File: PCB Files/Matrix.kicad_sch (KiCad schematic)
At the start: 64 parts

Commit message: Change MX32 to 1.25U in the schematic
No real changes to production files
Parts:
- MX32: footprint MX_Only:MXOnly-1U-NoLED -> MX_Only:MXOnly-1.25U-NoLED
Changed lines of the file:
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@@
       (effects (font (size 0.508 0.508)) (justify left))
     )
-    (property "Footprint" "MX_Only:MXOnly-1U-NoLED" (id 2) (at 156.591 149.098 0)
+    (property "Footprint" "MX_Only:MXOnly-1.25U-NoLED" (id 2) (at 156.591 149.098 0)
       (effects (font (size 1.524 1.524)) hide)
     )

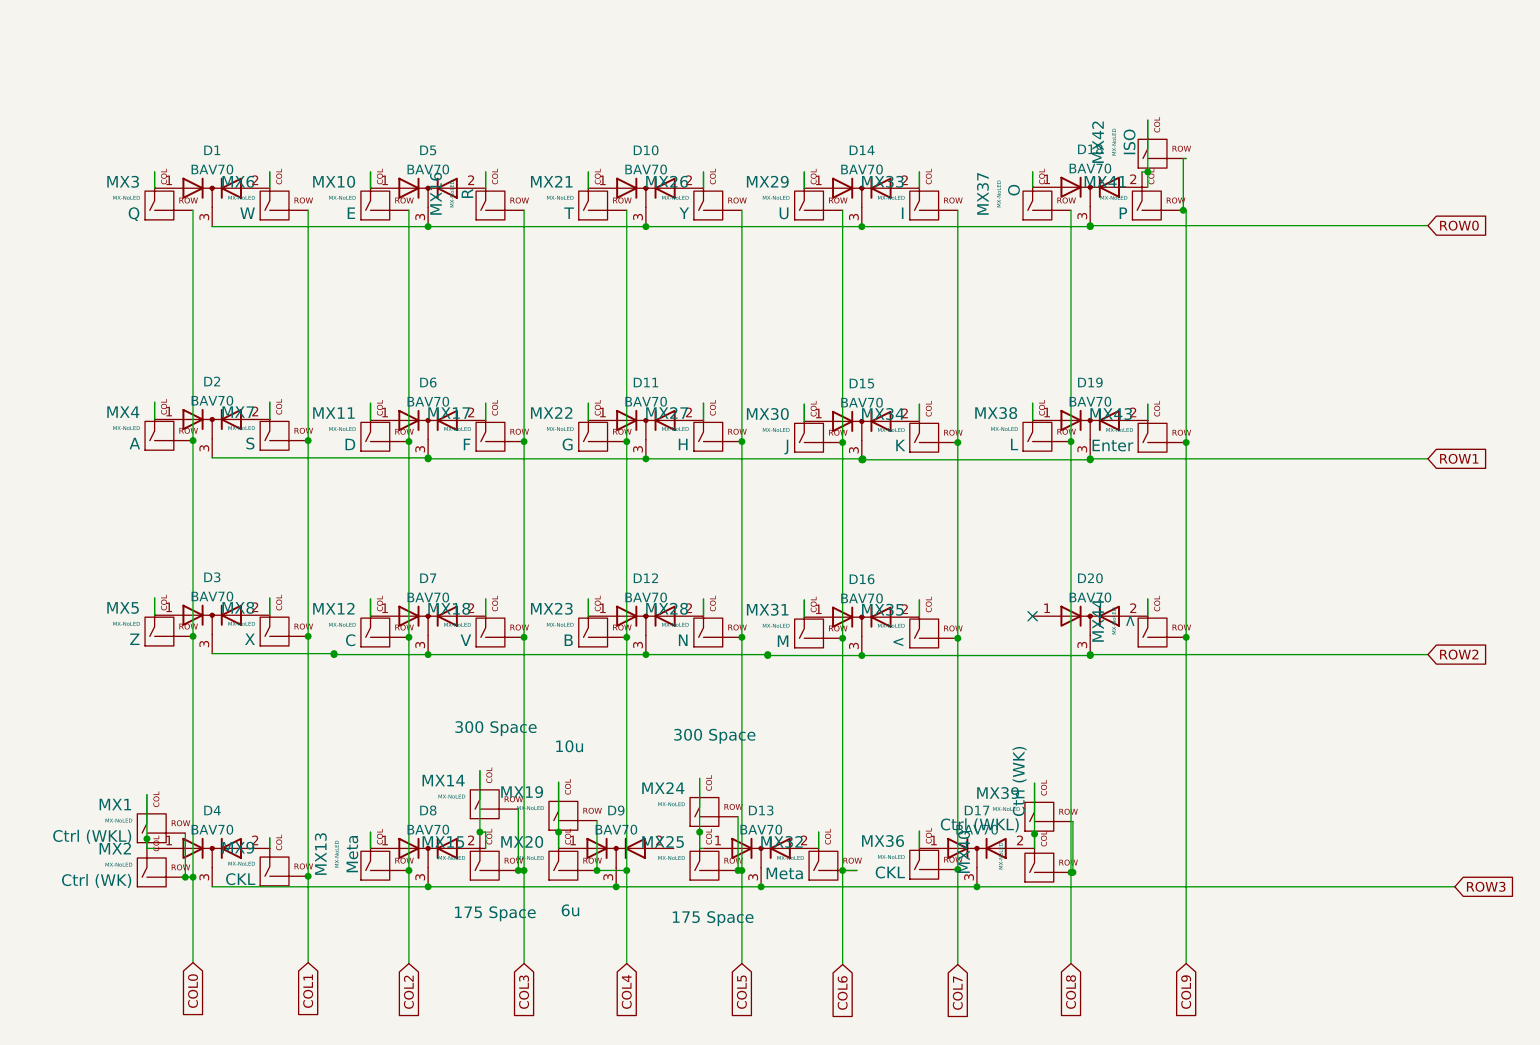
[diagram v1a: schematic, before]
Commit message: Cleanup the schematics and add a library for smaller bav70s
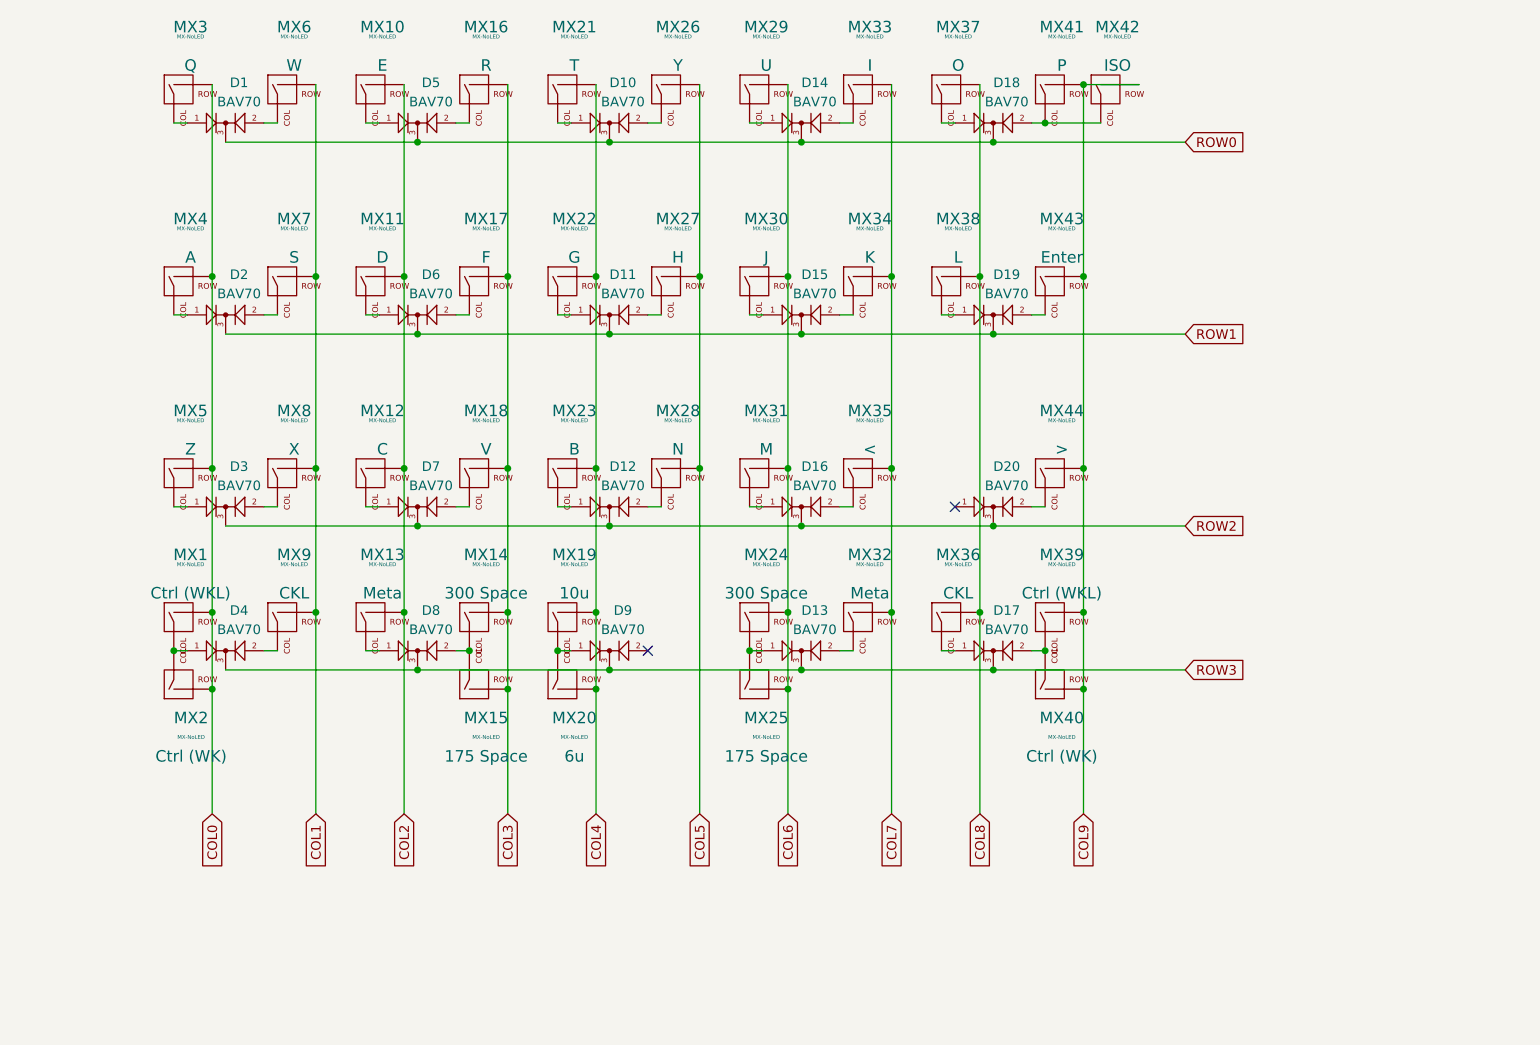
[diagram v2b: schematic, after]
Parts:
- D1, D10, D11, D12, D13, D14, D15, D16, D17, D18, D19, D2, D20, D3, D4, D5, D6, D7, D8, D9: symbol Diode:BAV70 -> marbastlib-various:BAV70_Small
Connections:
- net COL5: no longer MX24.2 (ROW), MX25.2 (ROW)
- net COL6: now also MX24.2 (ROW), MX25.2 (ROW); no longer MX32.2 (ROW)
- net COL7: now also MX32.2 (ROW); no longer MX36.2 (ROW)
- net COL8: now also MX36.2 (ROW); no longer MX39.2 (ROW), MX40.2 (ROW)
- net COL9: now also MX39.2 (ROW), MX40.2 (ROW)
- no-connect marks 1 -> 2
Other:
- moved on the sheet: MX1, MX10, MX11, MX12, MX13, MX14, MX15, MX16, MX17, MX18, MX19, MX2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

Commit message: Update dump
- Fix bottom row layout
- Add copium to dubba 1.75u shift using 1.5u and 1.25u
- Uglify @ASH-ART's routing
- Generate gerbers as recommended by JLC
- Add a logotype and revision number
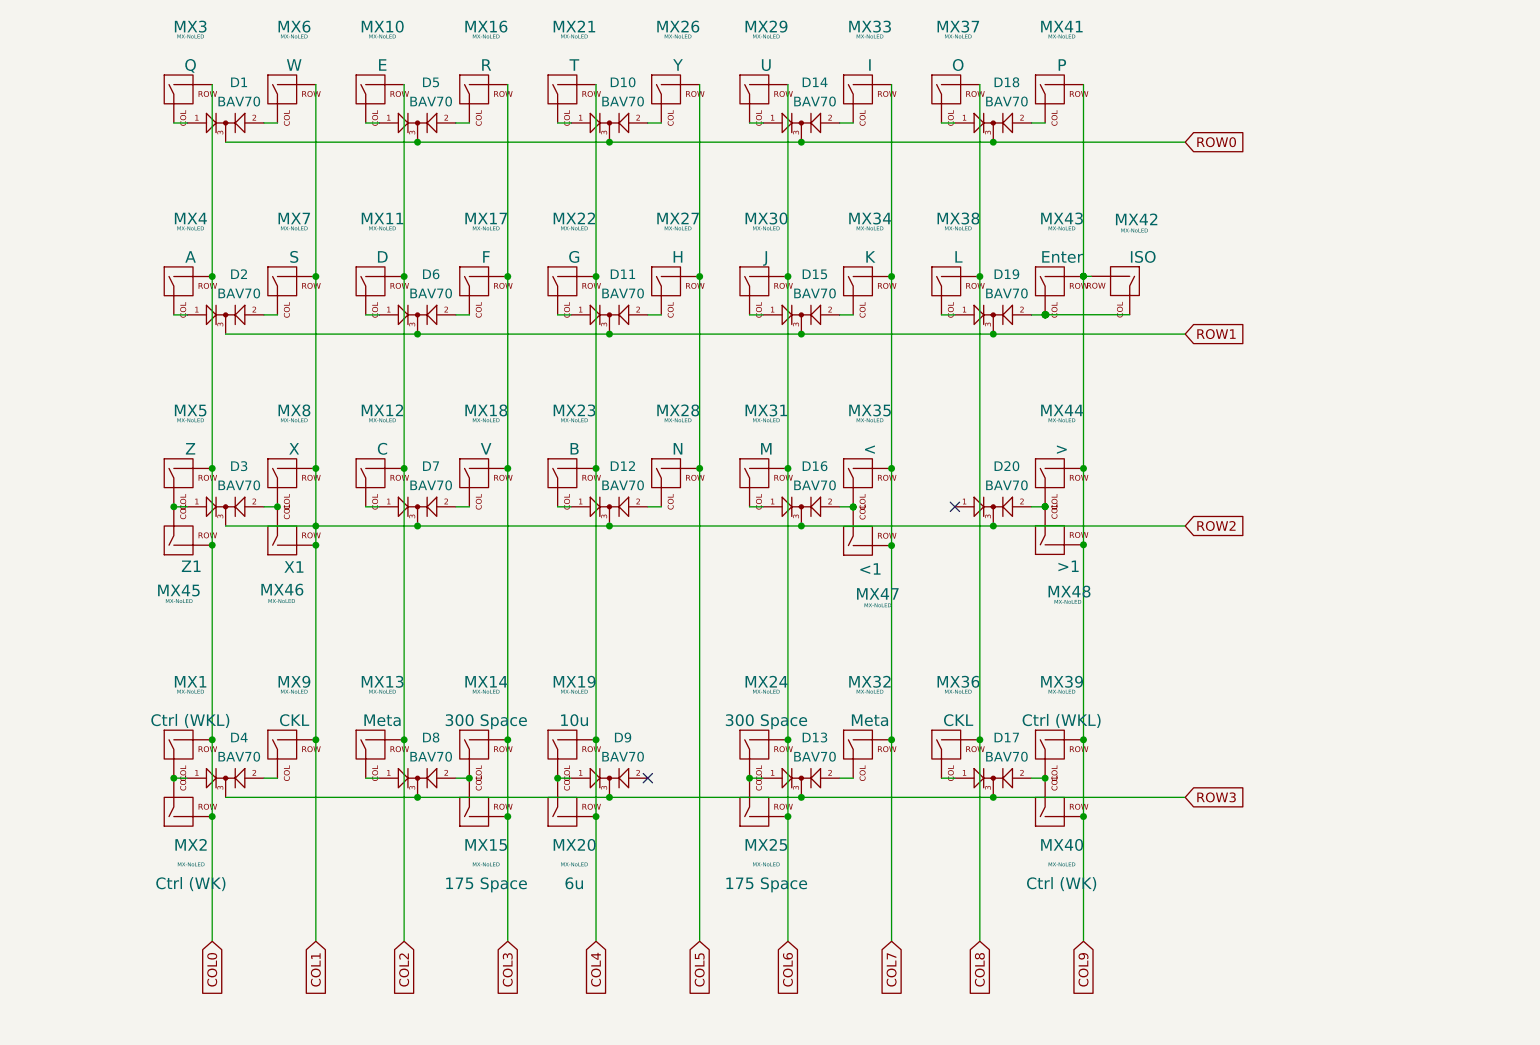
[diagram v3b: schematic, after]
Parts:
- added MX45, MX48: MX-NoLED, MX_Only:MXOnly-1.5U-NoLED, symbol MX_Alps_Hybrid:MX-NoLED
- added MX46, MX47: MX-NoLED, MX_Only:MXOnly-1.25U-NoLED, symbol MX_Alps_Hybrid:MX-NoLED
- D1, D10, D11, D12, D13, D14, D15, D16, D17, D18, D19, D2, D20, D3, D4, D5, D6, D7, D8, D9: LCSC (none) -> C2501
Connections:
- net ROW2 is gone; now on net COL1: D12.3 (K), D16.3 (K), D20.3 (K), D3.3 (K), D7.3 (K)
- net COL0: now also MX45.2 (ROW)
- net COL1: now also MX46.2 (ROW)
- net COL7: now also MX47.2 (ROW)
- net COL9: now also MX48.2 (ROW); no longer MX43.2 (ROW)
- net at D19.2 (A2), MX43.1 (COL): now also MX42.1 (COL)
- net at D18.2 (A2), MX41.1 (COL): no longer MX42.1 (COL)
- net at D20.2 (A2), MX44.1 (COL): now also MX48.1 (COL)
- net at D3.1 (A1), MX5.1 (COL): now also MX45.1 (COL)
- net at D3.2 (A2), MX8.1 (COL): now also MX46.1 (COL)
- net at D16.2 (A2), MX35.1 (COL): now also MX47.1 (COL)
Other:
- moved on the sheet: D13, D17, D4, D8, D9, MX1, MX13, MX14, MX15, MX19, MX2, MX20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
